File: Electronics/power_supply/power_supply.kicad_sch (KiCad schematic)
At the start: 76 parts, among them IC2 LM5069MMX-2_NOPB, J1 Conn_01x02_Male, J10 9801-0-15-15-23-27-10-0, J11 22-03-5035, J12 9801-0-15-15-23-27-10-0, J13 9801-0-15-15-23-27-10-0, J14 9801-0-15-15-23-27-10-0, J2 9801-0-15-15-23-27-10-0, J3 Conn_01x02_Male, J5 9801-0-15-15-23-27-10-0, J6 Conn_01x04_Male, J7 Conn_01x02_Male, J8 22-03-5035, Q1 IPD90N04S4L04ATMA1, Q2 PNP, U1 R-78B1.5-2.0, U2 INA226, U3 INA226

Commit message: Update PowerSupply PCB
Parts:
- removed C18, C4: 10uF, Capacitor_SMD:C_1206_3216Metric_Pad1.33x1.80mm_HandSolder, symbol Device:C
- removed C19, C5: 22uF, Capacitor_SMD:C_1206_3216Metric_Pad1.33x1.80mm_HandSolder, symbol Device:C
- removed H1, H2: MountingHole, MountingHole:MountingHole_3.2mm_M3, symbol Mechanical:MountingHole
- removed J11, J8: 22-03-5035, MiAM:SHDR3W60P0X250_1X3_990X490X590P, symbol MiAM:22-03-5035
- removed Q2: PNP, Package_TO_SOT_SMD:SOT-1123, symbol Simulation_SPICE:PNP
- added H5, H6: 9774030951R, MiAM:9774030951R, symbol MiAM:9774030951R
- added J4: 821-22-002-10-000101, MiAM:8212200210000101, symbol MiAM:821-22-002-10-000101
- added NT1: NetTie_2, NetTie:NetTie-2_SMD_Pad0.5mm, symbol Device:NetTie_2
- added Q3: BC857, Package_TO_SOT_SMD:SOT-23, symbol Transistor_BJT:BC857
- PS1: Mouser Part Number 894-APXW005A0X3-SRZ -> 894-APXW012A0X3-SRDZ
- R10: MPN RC0402FR-0710KL -> (none); RS 678-4697 -> 198-5597
- R7: value 6k -> 5k
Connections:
- net GND: now also NT1.2; no longer C25.2, C29.2, IC2.4 (OVLO), IC2.5 (GND), R10.2
- net SCL: now also J4.1
- net SDA: now also J4.2
- net VS: now also R8.3, R8.4; no longer R8.1, R8.2
- net at Q1.2 (D): now also R8.2; no longer R8.3
- net at IC2.1 (SENSE): now also R8.1; no longer R8.4
- net Vbat: now reaches C28.1, D4.1 (K), J1.2 (Pin_2), J7.1 (Pin_1), U1.1 (IN)
- net at R9.2: now also Q3.1 (B)
- net at C29.1, D5.1 (K): now also Q3.2 (E)
- new net GNDS: C25.2, C29.2, IC2.4 (OVLO), IC2.5 (GND), NT1.1, Q3.3 (C), R10.2
- no-connect marks 0 -> 1
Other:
- moved on the sheet: C25, C26, C27, C29, D1, D3, D5, IC2, J6, Q1, R10, R5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

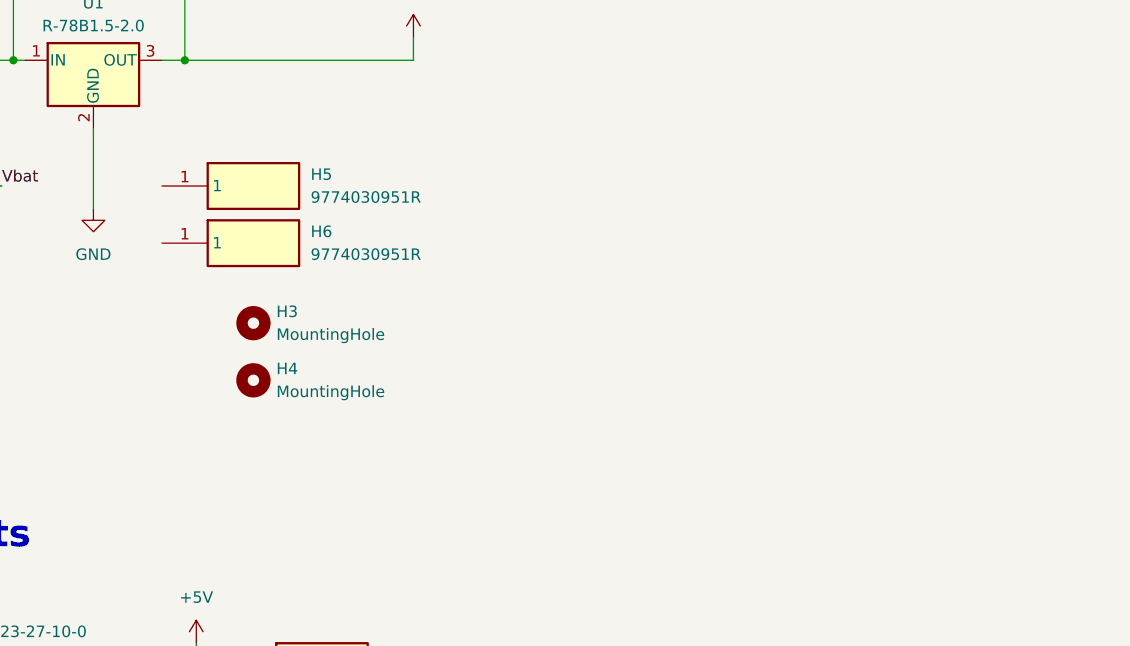
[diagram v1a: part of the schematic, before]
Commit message: PCB update - passes DRC
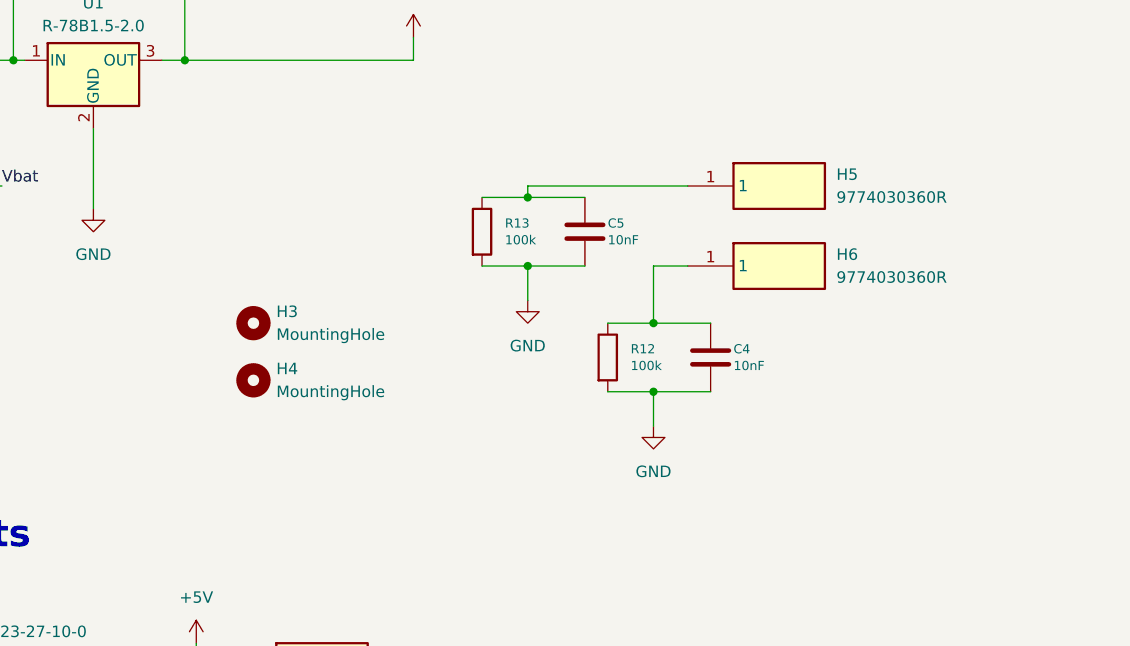
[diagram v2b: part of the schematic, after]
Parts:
- removed H5, H6: 9774030951R, MiAM:9774030951R, symbol MiAM:9774030951R
- added C4, C5: 10nF, Capacitor_SMD:C_0402_1005Metric_Pad0.74x0.62mm_HandSolder, symbol Device:C
- added H5, H6: 9774030360R, MiAM:9774030360R, symbol MiAM:9774030360R
- added R12, R13: 100k, Resistor_SMD:R_0402_1005Metric_Pad0.72x0.64mm_HandSolder, symbol Device:R
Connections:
- net GND: now also C4.2, C5.2, R12.2, R13.2
- new net: C5.1, H5.1, R13.1
- new net: C4.1, H6.1, R12.1

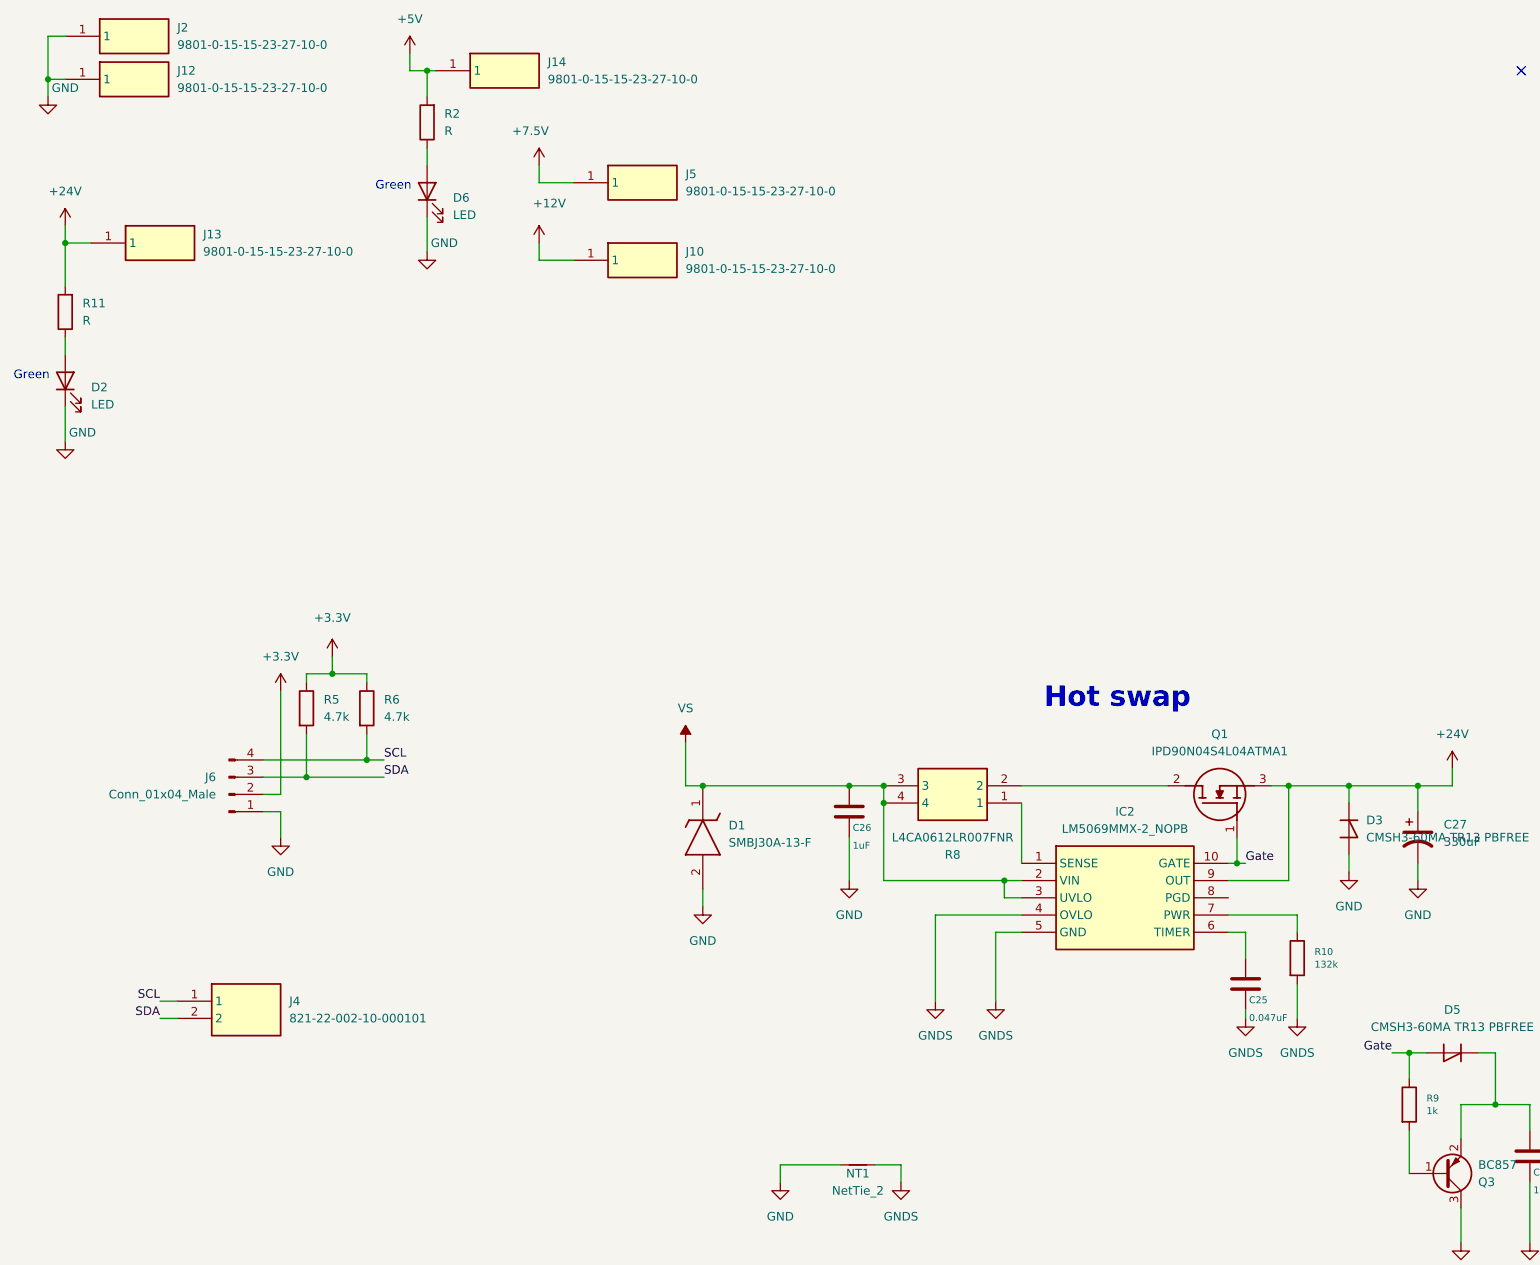
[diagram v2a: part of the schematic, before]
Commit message: PCB fixup + PCA9546A driver (WIP)
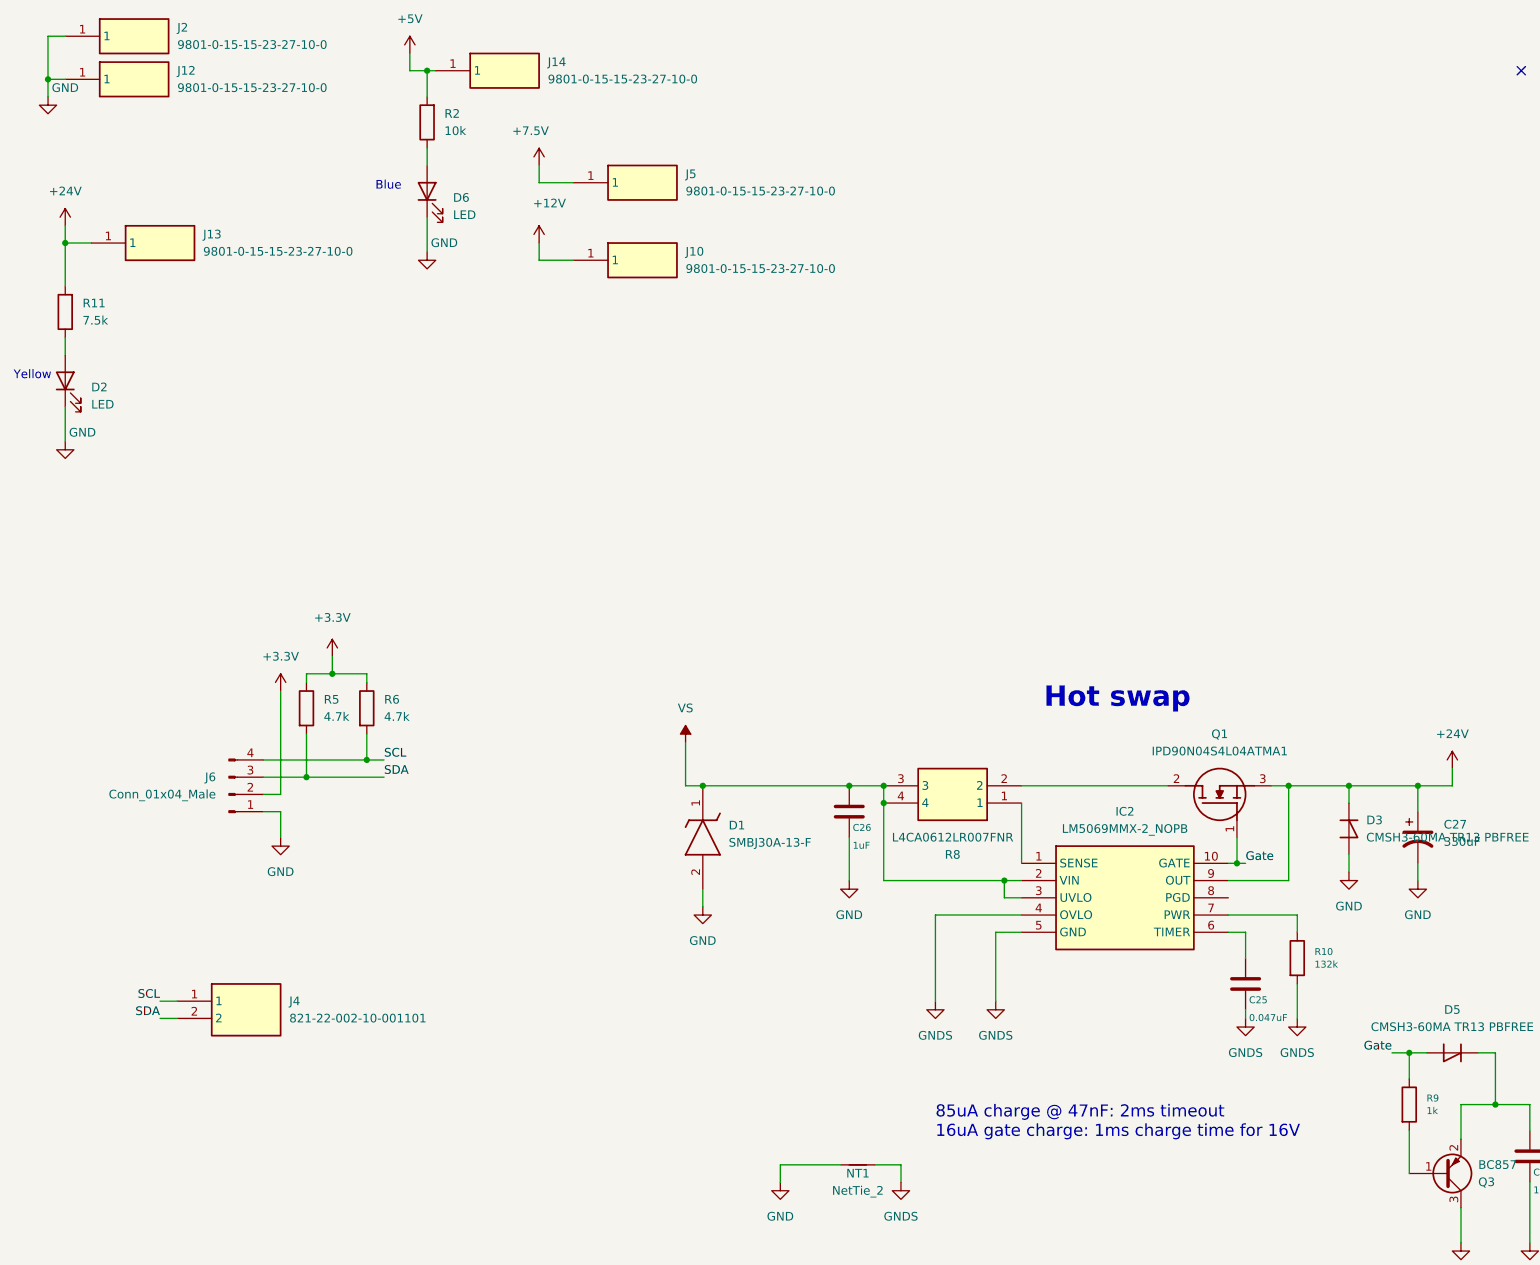
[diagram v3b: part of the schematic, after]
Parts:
- J4: value 821-22-002-10-000101 -> 821-22-002-10-001101; Manufacturer_Part_Number 821-22-002-10-000101 -> 821-22-002-10-001101; Mouser Part Number 575-8212200210000101 -> 575-8212200210001101
- R11: value R -> 7.5k
- R2: value R -> 10k
- R8: Mouser Part Number 71-WSL36377L000FEA -> 576-L4CA0612LR007FNR
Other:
- note added: "85uA charge @ 47nF: 2ms timeout 16uA gate charge: 1ms charge time for 16V"
- note added: "Blue"
- note added: "Yellow"
- note removed: "Green"
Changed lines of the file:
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@@
 		)
 	)
-	(text "Green"
+	(text "Blue"
 		(exclude_from_sim no)
 		(at 67.31 118.11 0)
@@
 		)
 	)
+	(text "85uA charge @ 47nF: 2ms timeout\n16uA gate charge: 1ms charge time for 16V"
+		(exclude_from_sim no)
+		(at 149.86 257.81 0)
+		(effects
+			(font
+				(size 1.778 1.778)
+			)
+			(justify left bottom)
+		)
+	)
 	(text "12V"
 		(exclude_from_sim no)
@@
 		)
 	)
-	(text "Green"
+	(text "Yellow"
 		(exclude_from_sim no)
 		(at 13.97 146.05 0)
@@
 			)
 		)
-		(property "Mouser Part Number" " 71-WSL36377L000FEA "
+		(property "Mouser Part Number" " 576-L4CA0612LR007FNR "
 			(at 146.05 -486.64 0)
 			(effects
@@
 			)
 		)
-		(property "Value" "821-22-002-10-000101"
+		(property "Value" "821-22-002-10-001101"
 			(at 54.61 240.0299 0)
 			(effects
@@
 			)
 		)
-		(property "Manufacturer_Part_Number" "821-22-002-10-000101"
+		(property "Manufacturer_Part_Number" "821-22-002-10-001101"
 			(at 54.61 832.41 0)
 			(effects
@@
 			)
 		)
-		(property "Mouser Part Number" "575-8212200210000101"
+		(property "Mouser Part Number" "575-8212200210001101"
 			(at 54.61 932.41 0)
 			(effects
@@
 			)
 		)
-		(property "Value" "R"
+		(property "Value" "10k"
 			(at 77.47 109.2199 0)
 			(effects
@@
 			)
 		)
-		(property "Value" "R"
+		(property "Value" "7.5k"
 			(at 24.13 137.1599 0)
 			(effects

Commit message: PCB fixup
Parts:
- J4: Manufacturer_Part_Number 821-22-002-10-001101 -> 821-22-002-10-000101
- R11: value 7.5k -> R
- R2: value 10k -> R
- R8: Mouser Part Number 576-L4CA0612LR007FNR -> 71-WSL36377L000FEA
- RA1, RA2: Mouser 504-MFSA1206R0080FCM -> 576-L4CA0612LR007FNR
- U1: value R-78B1.5-2.0 -> R-78B5.0-2.0; Mouser R-78B1.5-2.0 -> R-78B5.0-2.0
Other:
- note added: "Green"
- note removed: "85uA charge @ 47nF: 2ms timeout 16uA gate charge: 1ms charge time for 16V"
- note removed: "Blue"
- note removed: "Yellow"
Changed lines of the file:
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@@
 		)
 	)
-	(text "Blue"
+	(text "Green"
 		(exclude_from_sim no)
 		(at 67.31 118.11 0)
@@
 		)
 	)
-	(text "85uA charge @ 47nF: 2ms timeout\n16uA gate charge: 1ms charge time for 16V"
-		(exclude_from_sim no)
-		(at 149.86 257.81 0)
-		(effects
-			(font
-				(size 1.778 1.778)
-			)
-			(justify left bottom)
-		)
-	)
 	(text "12V"
 		(exclude_from_sim no)
@@
 		)
 	)
-	(text "Yellow"
+	(text "Green"
 		(exclude_from_sim no)
 		(at 13.97 146.05 0)
@@
 			)
 		)
-		(property "Mouser Part Number" " 576-L4CA0612LR007FNR "
+		(property "Mouser Part Number" " 71-WSL36377L000FEA "
 			(at 146.05 -486.64 0)
 			(effects
@@
 			)
 		)
-		(property "Manufacturer_Part_Number" "821-22-002-10-001101"
+		(property "Manufacturer_Part_Number" "821-22-002-10-000101"
 			(at 54.61 832.41 0)
 			(effects
@@
 			)
 		)
-		(property "Mouser" " 504-MFSA1206R0080FCM"
+		(property "Mouser" "576-L4CA0612LR007FNR "
 			(at 346.71 207.01 0)
 			(effects
@@
 			)
 		)
-		(property "Value" "10k"
+		(property "Value" "R"
 			(at 77.47 109.2199 0)
 			(effects
@@
 			)
 		)
-		(property "Value" "7.5k"
+		(property "Value" "R"
 			(at 24.13 137.1599 0)
 			(effects
@@
 			)
 		)
-		(property "Value" "R-78B1.5-2.0"
+		(property "Value" "R-78B5.0-2.0"
 			(at 60.96 29.21 0)
 			(effects
@@
 			)
 		)
-		(property "Mouser" "R-78B1.5-2.0"
+		(property "Mouser" "R-78B5.0-2.0"
 			(at 60.96 33.02 0)
 			(effects
@@
 			)
 		)
-		(property "Mouser" " 504-MFSA1206R0080FCM"
+		(property "Mouser" "576-L4CA0612LR007FNR "
 			(at 327.66 99.06 0)
 			(effects

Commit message: Rework rail motion through RailManager class
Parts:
- R8: Mouser Part Number 71-WSL36377L000FEA -> 576-L4CA0612LR007FNR
- RA1, RA2: Mouser 576-L4CA0612LR007FNR -> (none); Mouser Part Number (none) -> 504-MSMA1206R0080FCM
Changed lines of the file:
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@@
 	(label "Vout"
 		(at 327.66 85.09 0)
-		(fields_autoplaced yes)
 		(effects
 			(font
@@
 	(label "Vtrim"
 		(at 339.09 48.26 0)
-		(fields_autoplaced yes)
 		(effects
 			(font
@@
 	(label "Gate"
 		(at 195.58 217.17 0)
-		(fields_autoplaced yes)
 		(effects
 			(font
@@
 	(label "Vtrim12"
 		(at 337.82 161.29 0)
-		(fields_autoplaced yes)
 		(effects
 			(font
@@
 	(label "Vout"
 		(at 373.38 45.72 0)
-		(fields_autoplaced yes)
 		(effects
 			(font
@@
 	(label "Gate"
 		(at 217.17 245.11 180)
-		(fields_autoplaced yes)
 		(effects
 			(font
@@
 	(label "Vtrim12"
 		(at 383.54 163.83 180)
-		(fields_autoplaced yes)
 		(effects
 			(font
@@
 	(label "SDA"
 		(at 294.64 95.25 180)
-		(fields_autoplaced yes)
 		(effects
 			(font
@@
 	(label "SCL"
 		(at 68.58 201.93 0)
-		(fields_autoplaced yes)
 		(effects
 			(font
@@
 	(label "SDA"
 		(at 35.56 240.03 180)
-		(fields_autoplaced yes)
 		(effects
 			(font
@@
 	(label "SCL"
 		(at 294.64 97.79 180)
-		(fields_autoplaced yes)
 		(effects
 			(font
@@
 	(label "SCL"
 		(at 35.56 237.49 180)
-		(fields_autoplaced yes)
 		(effects
 			(font
@@
 	(label "Vsens"
 		(at 337.82 106.68 0)
-		(fields_autoplaced yes)
 		(effects
 			(font
@@
 	(label "Vtrim"
 		(at 384.81 50.8 180)
-		(fields_autoplaced yes)
 		(effects
 			(font
@@
 	(label "Vbat"
 		(at 50.8 46.99 0)
-		(fields_autoplaced yes)
 		(effects
 			(font
@@
 	(label "SDA"
 		(at 68.58 204.47 0)
-		(fields_autoplaced yes)
 		(effects
 			(font
@@
 	(label "Vout12"
 		(at 346.71 193.04 0)
-		(fields_autoplaced yes)
 		(effects
 			(font
@@
 	(label "Vout12"
 		(at 372.11 158.75 0)
-		(fields_autoplaced yes)
 		(effects
 			(font
@@
 	(label "SDA"
 		(at 313.69 203.2 180)
-		(fields_autoplaced yes)
 		(effects
 			(font
@@
 	(label "SCL"
 		(at 313.69 205.74 180)
-		(fields_autoplaced yes)
 		(effects
 			(font
@@
 			)
 		)
-		(property "Mouser Part Number" " 71-WSL36377L000FEA "
+		(property "Mouser Part Number" "576-L4CA0612LR007FNR "
 			(at 146.05 -486.64 0)
 			(effects
@@
 			)
 		)
-		(property "Mouser" "576-L4CA0612LR007FNR "
+		(property "Mouser Part Number" " 504-MSMA1206R0080FCM "
 			(at 346.71 207.01 0)
 			(effects
@@
 			)
 		)
-		(property "Mouser" "576-L4CA0612LR007FNR "
+		(property "Mouser Part Number" " 504-MSMA1206R0080FCM "
 			(at 327.66 99.06 0)
 			(effects

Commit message: [Elec] V2 of power supply
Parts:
- added C18, C19: 0.1uF, Capacitor_SMD:C_0805_2012Metric, symbol Device:C
- added IC1: TLV76033DBZR, MiAM:SOT95P237X112-3N, symbol MiAM:TLV76033DBZR
- added J8: Conn_01x02_Male, MiAM:XT30UM, symbol Connector:Conn_01x02_Male
- added J9: Conn_01x02_Pin, Connector_PinHeader_2.54mm:PinHeader_1x02_P2.54mm_Vertical, symbol Connector:Conn_01x02_Pin
- added RV3: 3314J-2-104E, Potentiometer_SMD:Potentiometer_Bourns_3314J_Vertical, symbol Device:R_Potentiometer
- added S1: 7813J-1-051E, MiAM:7813J1051E, symbol MiAM:7813J-1-051E
- C11, C13, C23, C25, C9: value 0.047uF -> 47nF
- C12, C17: footprint Capacitor_SMD:C_0402_1005Metric_Pad0.74x0.62mm_HandSolder -> Capacitor_SMD:C_0805_2012Metric; HOUSEPART YES -> (none); MPN MF-CAP-0402-0.1uF -> (none); RS 247-7824 -> (none)
- C4, C5: footprint Capacitor_SMD:C_0402_1005Metric_Pad0.74x0.62mm_HandSolder -> Capacitor_SMD:C_0805_2012Metric; HOUSEPART 1 -> (none); MPN MF-CAP-0402-1nF -> (none); POPULATE 1 -> (none)
- D3, D4, D5: value CMSH3-60MA TR13 PBFREE -> SS14; footprint Diode_SMD:D_SMA -> MiAM:DIONM5327X242N; Mouser 610-CMSH3-60MA-TR13 -> (none)
- H5, H6, J4: now not fitted
- PS1, PS2: footprint MiAM:APXW012A0X3SRDZ -> MiAM:APXW012A0X3SRDZ_TH
- R10: value 132k -> 100k; MF Yageo -> (none); RS 198-5597 -> (none)
- R11, R2: value R -> 5k
- R12, R13: footprint Resistor_SMD:R_0402_1005Metric_Pad0.72x0.64mm_HandSolder -> Resistor_SMD:R_0805_2012Metric; HOUSEPART YES -> (none); MPN MF-RES-0402-2K -> (none)
- R4: value 6k -> 6.8k
- R7: value 5k -> 4.7k
- RV1: value 10k -> 652-3314J-2-103E; Mouser (none) -> 652-3314J-2-103E
- RV2: value 10k -> 3314J-2-103E; Mouser (none) -> 652-3314J-2-103E
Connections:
- net +24V: now also J8.1 (Pin_1)
- net +3.3V: now also C19.1, IC1.1 (OUT)
- net +5V: now also C18.1, IC1.2 (IN), J9.1 (Pin_1)
- net GND: now also C18.2, C19.2, IC1.3 (GND), J8.2 (Pin_2), J9.2 (Pin_2)
- net GNDS: now also RV3.2, RV3.3; no longer R10.2
- net Gate: now also S1.1 (CCW); no longer Q1.1 (G)
- net VS: no longer IC2.2 (VIN), IC2.3 (UVLO), R8.4
- net at Q1.2 (D), R8.2: now also S1.3 (CW)
- new net: IC2.2 (VIN), IC2.3 (UVLO), R8.4
- new net: R10.2, RV3.1
- new net: Q1.1 (G), S1.2 (C)
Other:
- moved on the sheet: C25, C29, Q1, Q3, R9
